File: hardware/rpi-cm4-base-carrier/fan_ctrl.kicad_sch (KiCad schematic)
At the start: 14 parts, among them IC6 EMC2305-1-AP-TR, IC7 LM2940S-12_NOPB, J15 47053-1000, J16 47053-1000, J17 47053-1000, J7 47053-1000

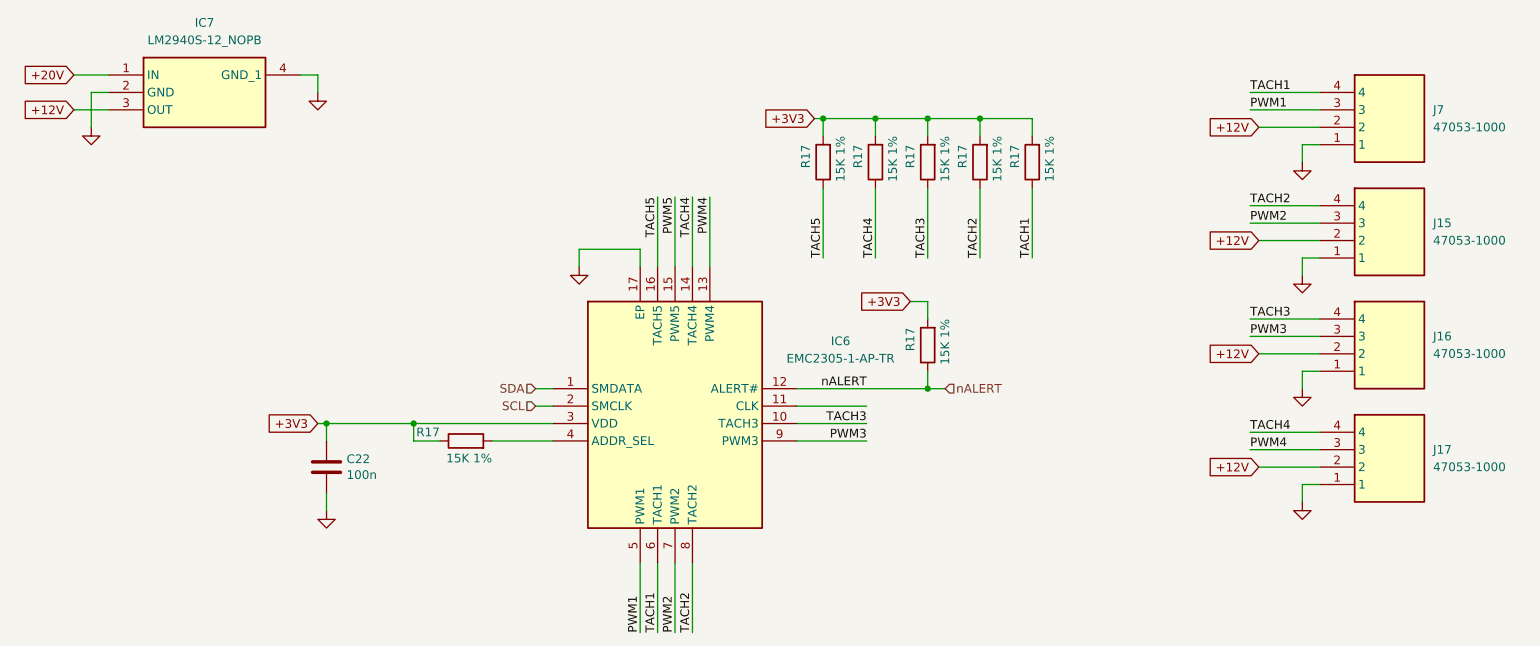
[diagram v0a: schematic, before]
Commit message: convert IC refs to U refs and re-annotate, add fiducials and extra via stitching to layout
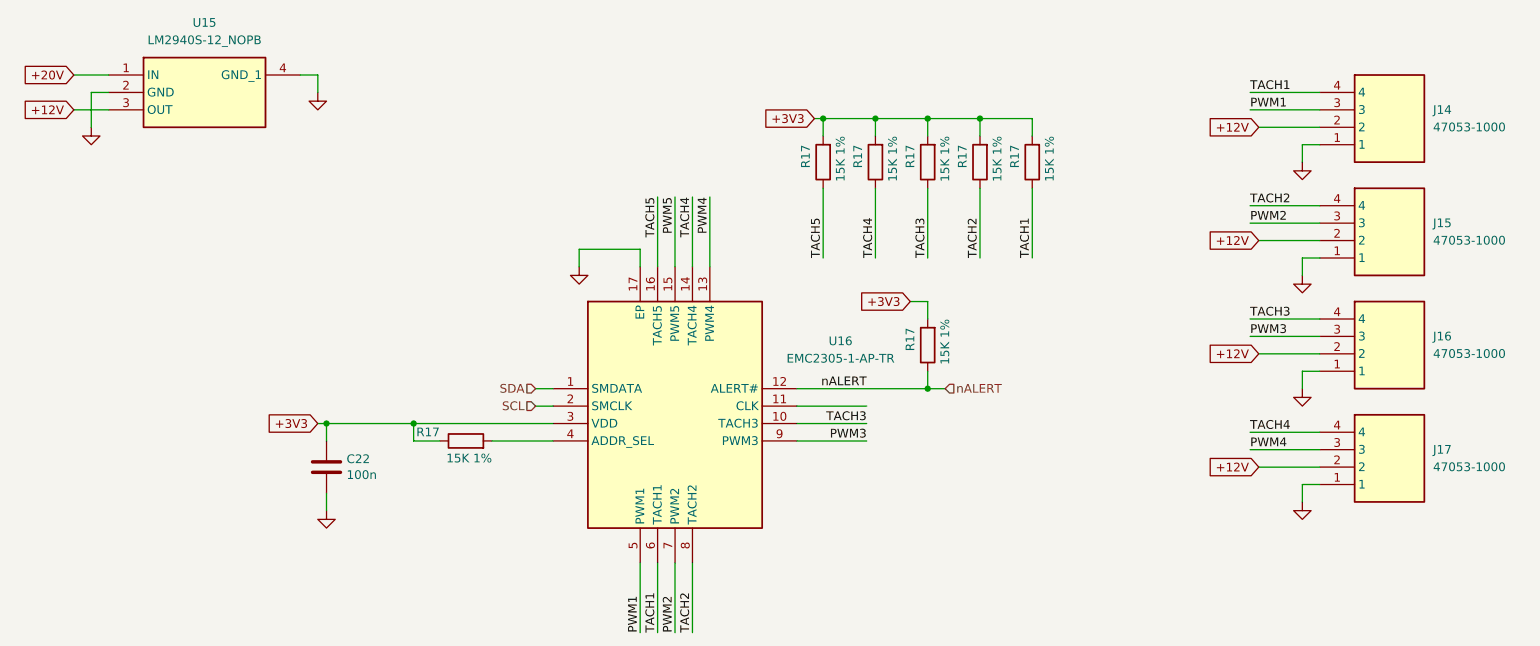
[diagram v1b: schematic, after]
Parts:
- renumbered J7 to J14, IC7 to U15, IC6 to U16
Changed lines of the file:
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@@
   (symbol (lib_id "SamacSys_Parts:EMC2305-1-AP-TR") (at 119.38 91.44 0) (unit 1)
     (in_bom yes) (on_board yes) (dnp no) (fields_autoplaced)
-    (property "Reference" "IC6" (at 161.29 84.5119 0)
+    (property "Reference" "U16" (at 161.29 84.5119 0)
       (effects (font (size 1.27 1.27)))
     )
@@
       (project "rpi-cm4-base-carrier"
         (path "/92c58705-ecb0-498b-b561-44a3f0daad57/fc4c71a5-1008-4ac4-98db-57c838c57d91/401a7b23-34b9-48d8-be17-7a989e62fb7e"
-          (reference "IC6") (unit 1)
+          (reference "U16") (unit 1)
         )
       )
@@
         )
         (path "/92c58705-ecb0-498b-b561-44a3f0daad57/fc4c71a5-1008-4ac4-98db-57c838c57d91/401a7b23-34b9-48d8-be17-7a989e62fb7e"
-          (reference "#PWR093") (unit 1)
+          (reference "#PWR094") (unit 1)
         )
       )
@@
   (symbol (lib_id "SamacSys_Parts:LM2940S-12_NOPB") (at 54.61 45.72 0) (unit 1)
     (in_bom yes) (on_board yes) (dnp no) (fields_autoplaced)
-    (property "Reference" "IC7" (at 68.58 38.1 0)
+    (property "Reference" "U15" (at 68.58 38.1 0)
       (effects (font (size 1.27 1.27)))
     )
@@
       (project "rpi-cm4-base-carrier"
         (path "/92c58705-ecb0-498b-b561-44a3f0daad57/fc4c71a5-1008-4ac4-98db-57c838c57d91/401a7b23-34b9-48d8-be17-7a989e62fb7e"
-          (reference "IC7") (unit 1)
+          (reference "U15") (unit 1)
         )
       )
@@
         )
         (path "/92c58705-ecb0-498b-b561-44a3f0daad57/fc4c71a5-1008-4ac4-98db-57c838c57d91/401a7b23-34b9-48d8-be17-7a989e62fb7e"
-          (reference "R45") (unit 1)
+          (reference "R44") (unit 1)
         )
       )
@@
         )
         (path "/92c58705-ecb0-498b-b561-44a3f0daad57/fc4c71a5-1008-4ac4-98db-57c838c57d91/401a7b23-34b9-48d8-be17-7a989e62fb7e"
-          (reference "#PWR097") (unit 1)
+          (reference "#PWR099") (unit 1)
         )
       )
@@
         )
         (path "/92c58705-ecb0-498b-b561-44a3f0daad57/fc4c71a5-1008-4ac4-98db-57c838c57d91/401a7b23-34b9-48d8-be17-7a989e62fb7e"
-          (reference "#PWR098") (unit 1)
+          (reference "#PWR092") (unit 1)
         )
       )
@@
         )
         (path "/92c58705-ecb0-498b-b561-44a3f0daad57/fc4c71a5-1008-4ac4-98db-57c838c57d91/401a7b23-34b9-48d8-be17-7a989e62fb7e"
-          (reference "#PWR094") (unit 1)
+          (reference "#PWR096") (unit 1)
         )
       )
@@
         )
         (path "/92c58705-ecb0-498b-b561-44a3f0daad57/fc4c71a5-1008-4ac4-98db-57c838c57d91/401a7b23-34b9-48d8-be17-7a989e62fb7e"
-          (reference "#PWR099") (unit 1)
+          (reference "#PWR093") (unit 1)
         )
       )
@@
         )
         (path "/92c58705-ecb0-498b-b561-44a3f0daad57/fc4c71a5-1008-4ac4-98db-57c838c57d91/401a7b23-34b9-48d8-be17-7a989e62fb7e"
-          (reference "R7") (unit 1)
+          (reference "R42") (unit 1)
         )
       )
@@
         )
         (path "/92c58705-ecb0-498b-b561-44a3f0daad57/fc4c71a5-1008-4ac4-98db-57c838c57d91/401a7b23-34b9-48d8-be17-7a989e62fb7e"
-          (reference "R8") (unit 1)
+          (reference "R46") (unit 1)
         )
       )
@@
         )
         (path "/92c58705-ecb0-498b-b561-44a3f0daad57/fc4c71a5-1008-4ac4-98db-57c838c57d91/401a7b23-34b9-48d8-be17-7a989e62fb7e"
-          (reference "R44") (unit 1)
+          (reference "R43") (unit 1)
         )
       )
@@
         )
         (path "/92c58705-ecb0-498b-b561-44a3f0daad57/fc4c71a5-1008-4ac4-98db-57c838c57d91/401a7b23-34b9-48d8-be17-7a989e62fb7e"
-          (reference "R46") (unit 1)
+          (reference "R45") (unit 1)
         )
       )
@@
         )
         (path "/92c58705-ecb0-498b-b561-44a3f0daad57/fc4c71a5-1008-4ac4-98db-57c838c57d91/401a7b23-34b9-48d8-be17-7a989e62fb7e"
-          (reference "#PWR096") (unit 1)
+          (reference "#PWR098") (unit 1)
         )
       )
@@
   (symbol (lib_id "SamacSys_Parts:47053-1000") (at 231.14 48.26 0) (unit 1)
     (in_bom yes) (on_board yes) (dnp no) (fields_autoplaced)
-    (property "Reference" "J7" (at 247.65 50.8 0)
+    (property "Reference" "J14" (at 247.65 50.8 0)
       (effects (font (size 1.27 1.27)) (justify left))
     )
@@
       (project "rpi-cm4-base-carrier"
         (path "/92c58705-ecb0-498b-b561-44a3f0daad57/fc4c71a5-1008-4ac4-98db-57c838c57d91/401a7b23-34b9-48d8-be17-7a989e62fb7e"
-          (reference "J7") (unit 1)
+          (reference "J14") (unit 1)
         )
       )
@@
         )
         (path "/92c58705-ecb0-498b-b561-44a3f0daad57/fc4c71a5-1008-4ac4-98db-57c838c57d91/401a7b23-34b9-48d8-be17-7a989e62fb7e"
-          (reference "#PWR092") (unit 1)
+          (reference "#PWR095") (unit 1)
         )
       )
@@
         )
         (path "/92c58705-ecb0-498b-b561-44a3f0daad57/fc4c71a5-1008-4ac4-98db-57c838c57d91/401a7b23-34b9-48d8-be17-7a989e62fb7e"
-          (reference "#PWR095") (unit 1)
-        )
-      )
+          (reference "#PWR097") (unit 1)
+        )
+      )

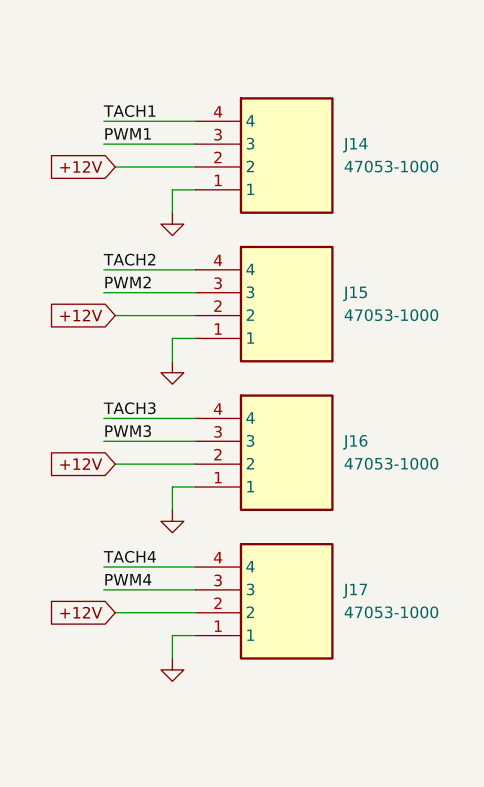
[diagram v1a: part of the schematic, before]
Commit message: design files exported ready for manufacture, LCSC part numbers added throughout the library
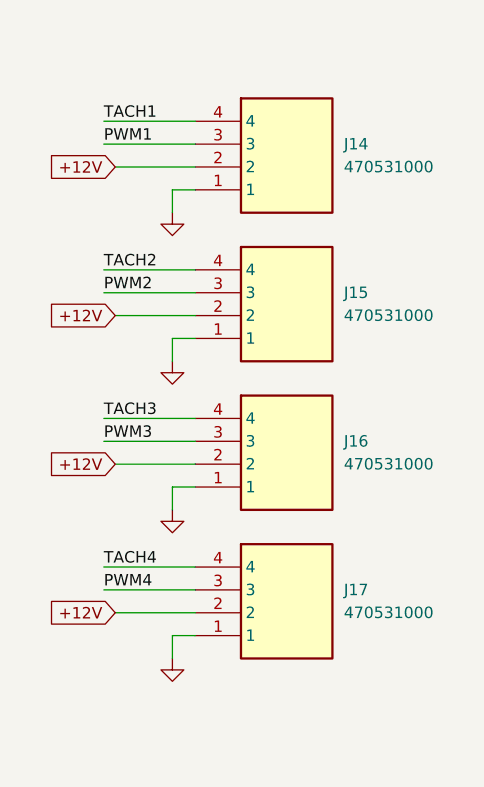
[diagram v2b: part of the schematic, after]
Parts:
- C22: LCSC Part # (none) -> C152724; LCSC Part Number (none) -> C152724
- J14, J15, J16, J17: value 47053-1000 -> 470531000; LCSC Part # (none) -> C240840; LCSC Part Number (none) -> C240840
- R17: LCSC Part # (none) -> C2576181; LCSC Part Number (none) -> C2576181
- U15: LCSC Part # (none) -> C2877347; LCSC Part Number (none) -> C2877347
- U16: LCSC Part # (none) -> C621415; LCSC Part Number (none) -> C621415
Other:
- title: (none) -> Raspberry Pi Compute Module 4 Control Node
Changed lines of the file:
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@@
 (kicad_sch (version 20230121) (generator eeschema)
   (paper "A4")
+  (title_block
+    (title "Raspberry Pi Compute Module 4 Control Node")
+    (date "2024-02-04")
+    (comment 2 "creativecommons.org/licenses/by-sa/4.0/")
+    (comment 3 "License: CC BY-SA 4.0")
+    (comment 4 "Author: Sam Earnshaw")
+  )
   (junction (at 181.61 52.07) (diameter 0) (color 0 0 0 0)
   )
@@
       (effects (font (size 1.27 1.27)) hide)
     )
+    (property "LCSC Part Number" "C2576181" (at 181.61 58.42 0)
+      (effects (font (size 1.27 1.27)) hide)
+    )
+    (property "LCSC Part #" "C2576181" (at 181.61 58.42 0)
+      (effects (font (size 1.27 1.27)) hide)
+    )
     (pin "1")
     (pin "2")
@@
     (property "Manufacturer_Part_Number" "EMC2305-1-AP-TR" (at 151.13 876.2 0)
       (effects (font (size 1.27 1.27)) (justify left top) hide)
+    )
+    (property "LCSC Part Number" "C621415" (at 119.38 91.44 0)
+      (effects (font (size 1.27 1.27)) hide)
+    )
+    (property "LCSC Part #" "C621415" (at 119.38 91.44 0)
+      (effects (font (size 1.27 1.27)) hide)
     )
     (pin "14")
@@
       (effects (font (size 1.27 1.27)) (justify left top) hide)
     )
+    (property "LCSC Part Number" "C2877347" (at 54.61 45.72 0)
+      (effects (font (size 1.27 1.27)) hide)
+    )
+    (property "LCSC Part #" "C2877347" (at 54.61 45.72 0)
+      (effects (font (size 1.27 1.27)) hide)
+    )
     (pin "4")
     (pin "3")
@@
     )
     (property "Field8" "120891581" (at 189.23 58.42 0)
+      (effects (font (size 1.27 1.27)) hide)
+    )
+    (property "LCSC Part Number" "C2576181" (at 189.23 58.42 0)
+      (effects (font (size 1.27 1.27)) hide)
+    )
+    (property "LCSC Part #" "C2576181" (at 189.23 58.42 0)
       (effects (font (size 1.27 1.27)) hide)
     )
@@
       (effects (font (size 1.27 1.27)) (justify left))
     )
-    (property "Value" "47053-1000" (at 247.65 102.87 0)
+    (property "Value" "470531000" (at 247.65 102.87 0)
       (effects (font (size 1.27 1.27)) (justify left))
     )
@@
     (property "Manufacturer_Part_Number" "47053-1000" (at 247.65 892.71 0)
       (effects (font (size 1.27 1.27)) (justify left top) hide)
+    )
+    (property "LCSC Part Number" "C240840" (at 231.14 97.79 0)
+      (effects (font (size 1.27 1.27)) hide)
+    )
+    (property "LCSC Part #" "C240840" (at 231.14 97.79 0)
+      (effects (font (size 1.27 1.27)) hide)
     )
     (pin "2")
@@
     )
     (property "Field8" "120891581" (at 166.37 58.42 0)
+      (effects (font (size 1.27 1.27)) hide)
+    )
+    (property "LCSC Part Number" "C2576181" (at 166.37 58.42 0)
+      (effects (font (size 1.27 1.27)) hide)
+    )
+    (property "LCSC Part #" "C2576181" (at 166.37 58.42 0)
       (effects (font (size 1.27 1.27)) hide)
     )
@@
       (effects (font (size 1.27 1.27)) hide)
     )
+    (property "LCSC Part Number" "C2576181" (at 106.68 99.06 0)
+      (effects (font (size 1.27 1.27)) hide)
+    )
+    (property "LCSC Part #" "C2576181" (at 106.68 99.06 0)
+      (effects (font (size 1.27 1.27)) hide)
+    )
     (pin "1")
     (pin "2")
@@
       (effects (font (size 1.27 1.27)) hide)
     )
+    (property "LCSC Part Number" "C152724" (at 86.36 102.87 0)
+      (effects (font (size 1.27 1.27)) hide)
+    )
+    (property "LCSC Part #" "C152724" (at 86.36 102.87 0)
+      (effects (font (size 1.27 1.27)) hide)
+    )
     (pin "1")
     (pin "2")
@@
       (effects (font (size 1.27 1.27)) hide)
     )
+    (property "LCSC Part Number" "C2576181" (at 173.99 85.09 0)
+      (effects (font (size 1.27 1.27)) hide)
+    )
+    (property "LCSC Part #" "C2576181" (at 173.99 85.09 0)
+      (effects (font (size 1.27 1.27)) hide)
+    )
     (pin "1")
     (pin "2")
@@
       (effects (font (size 1.27 1.27)) (justify left))
     )
-    (property "Value" "47053-1000" (at 247.65 86.36 0)
+    (property "Value" "470531000" (at 247.65 86.36 0)
       (effects (font (size 1.27 1.27)) (justify left))
     )
@@
     (property "Manufacturer_Part_Number" "47053-1000" (at 247.65 876.2 0)
       (effects (font (size 1.27 1.27)) (justify left top) hide)
+    )
+    (property "LCSC Part Number" "C240840" (at 231.14 81.28 0)
+      (effects (font (size 1.27 1.27)) hide)
+    )
+    (property "LCSC Part #" "C240840" (at 231.14 81.28 0)
+      (effects (font (size 1.27 1.27)) hide)
     )
     (pin "2")
@@
     )
     (property "Field8" "120891581" (at 158.75 58.42 0)
+      (effects (font (size 1.27 1.27)) hide)
+    )
+    (property "LCSC Part Number" "C2576181" (at 158.75 58.42 0)
+      (effects (font (size 1.27 1.27)) hide)
+    )
+    (property "LCSC Part #" "C2576181" (at 158.75 58.42 0)
       (effects (font (size 1.27 1.27)) hide)
     )
@@
       (effects (font (size 1.27 1.27)) hide)
     )
+    (property "LCSC Part Number" "C2576181" (at 173.99 58.42 0)
+      (effects (font (size 1.27 1.27)) hide)
+    )
+    (property "LCSC Part #" "C2576181" (at 173.99 58.42 0)
+      (effects (font (size 1.27 1.27)) hide)
+    )
     (pin "1")
     (pin "2")
@@
       (effects (font (size 1.27 1.27)) (justify left))
     )
-    (property "Value" "47053-1000" (at 247.65 53.34 0)
+    (property "Value" "470531000" (at 247.65 53.34 0)
       (effects (font (size 1.27 1.27)) (justify left))
     )
@@
     (property "Manufacturer_Part_Number" "47053-1000" (at 247.65 843.18 0)
       (effects (font (size 1.27 1.27)) (justify left top) hide)
+    )
+    (property "LCSC Part Number" "C240840" (at 231.14 48.26 0)
+      (effects (font (size 1.27 1.27)) hide)
+    )
+    (property "LCSC Part #" "C240840" (at 231.14 48.26 0)
+      (effects (font (size 1.27 1.27)) hide)
     )
     (pin "2")
@@
       (effects (font (size 1.27 1.27)) (justify left))
     )
-    (property "Value" "47053-1000" (at 247.65 69.85 0)
+    (property "Value" "470531000" (at 247.65 69.85 0)
       (effects (font (size 1.27 1.27)) (justify left))
     )
@@
       (effects (font (size 1.27 1.27)) (justify left top) hide)
     )
-    (pin "2")
+    (property "LCSC Part Number" "C240840" (at 231.14 64.77 0)
+      (effects (font (size 1.27 1.27)) hide)
+    )
+    (property "LCSC Part #" "C240840" (at 231.14 64.77 0)
+      (effects (font (size 1.27 1.27)) hide)
+    )
+    (pin "2")
